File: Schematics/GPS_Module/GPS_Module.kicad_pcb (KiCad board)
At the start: 2 copper layers, 20.3 x 8.4 mm, 86 parts, among them J1 Stack Male Edge Connector, J2 SWD_01x04_Pin, J3 25SH-B-06-TR, J4 25SH-B-06-TR, J6 USB_B_Micro, Q1 AO3400A, SW1 SW_STM_RESET, SW2 SW_STM_BOOT_MODE, U1 STM32F103CBTx, U10 AMS1117-3.3, U2 SAM-M10Q, U3 W25Q128JVS, U4 LM66100DCKR, U5 LM66100DCKR, U6 LM66100DCKR, U7 ACS70331EOLC, U8 LM66100DCKR, U9 ISO1042BQDWVR, Y1 X322516MMB4SI

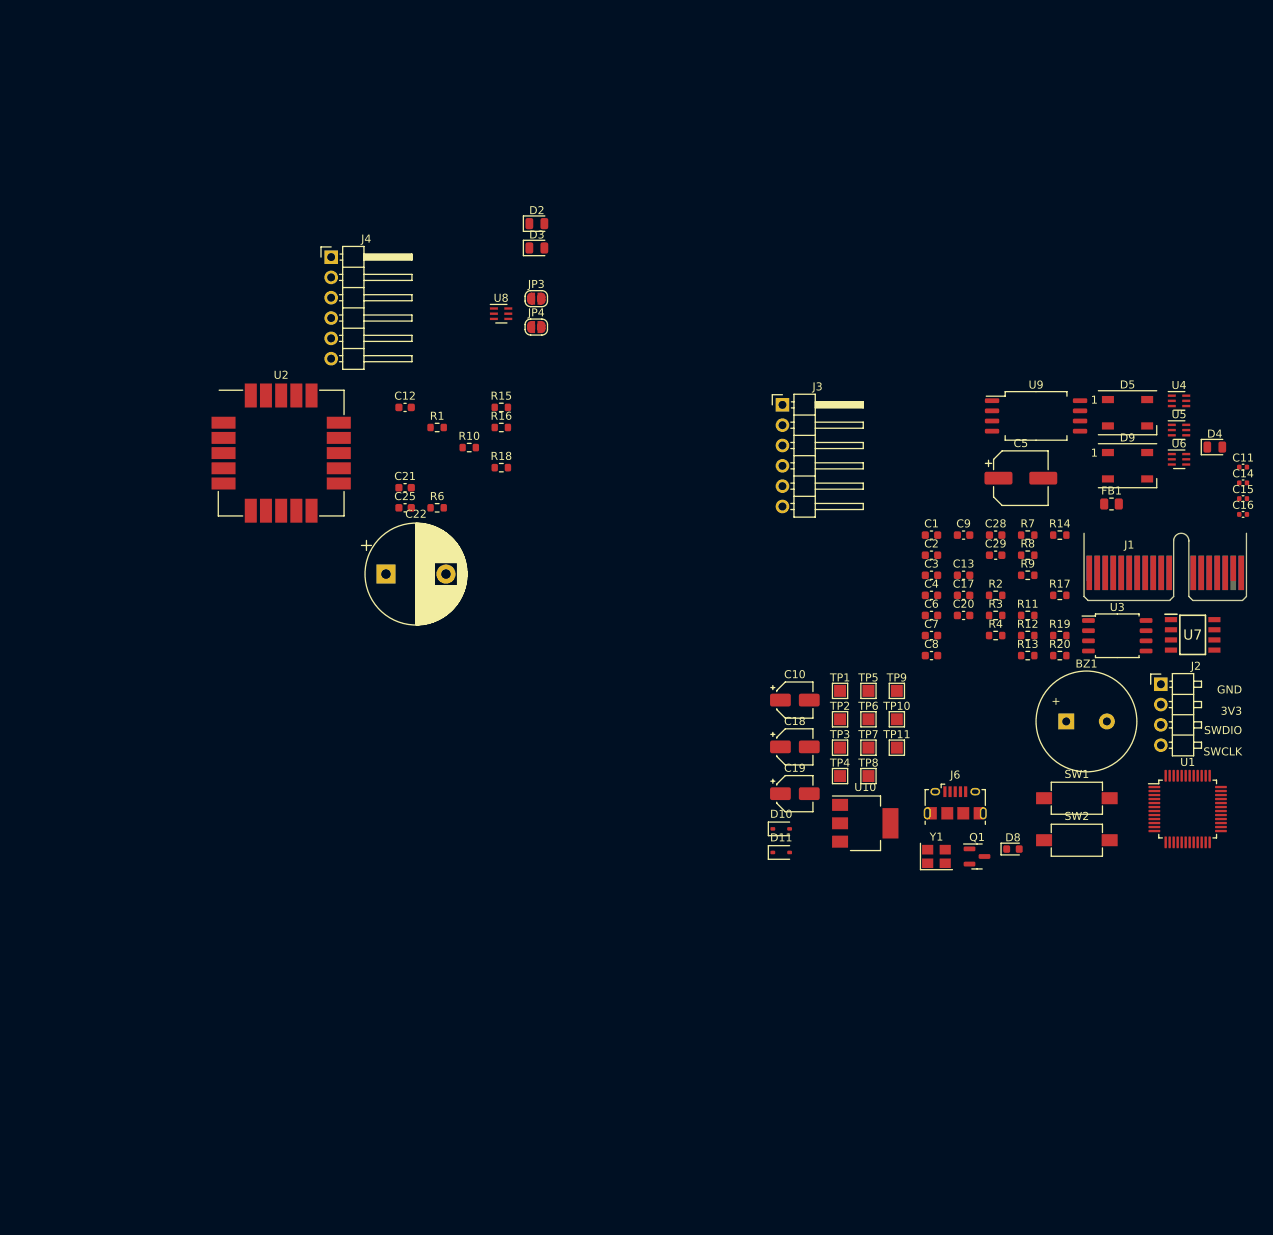
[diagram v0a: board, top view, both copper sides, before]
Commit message: Added PCB template
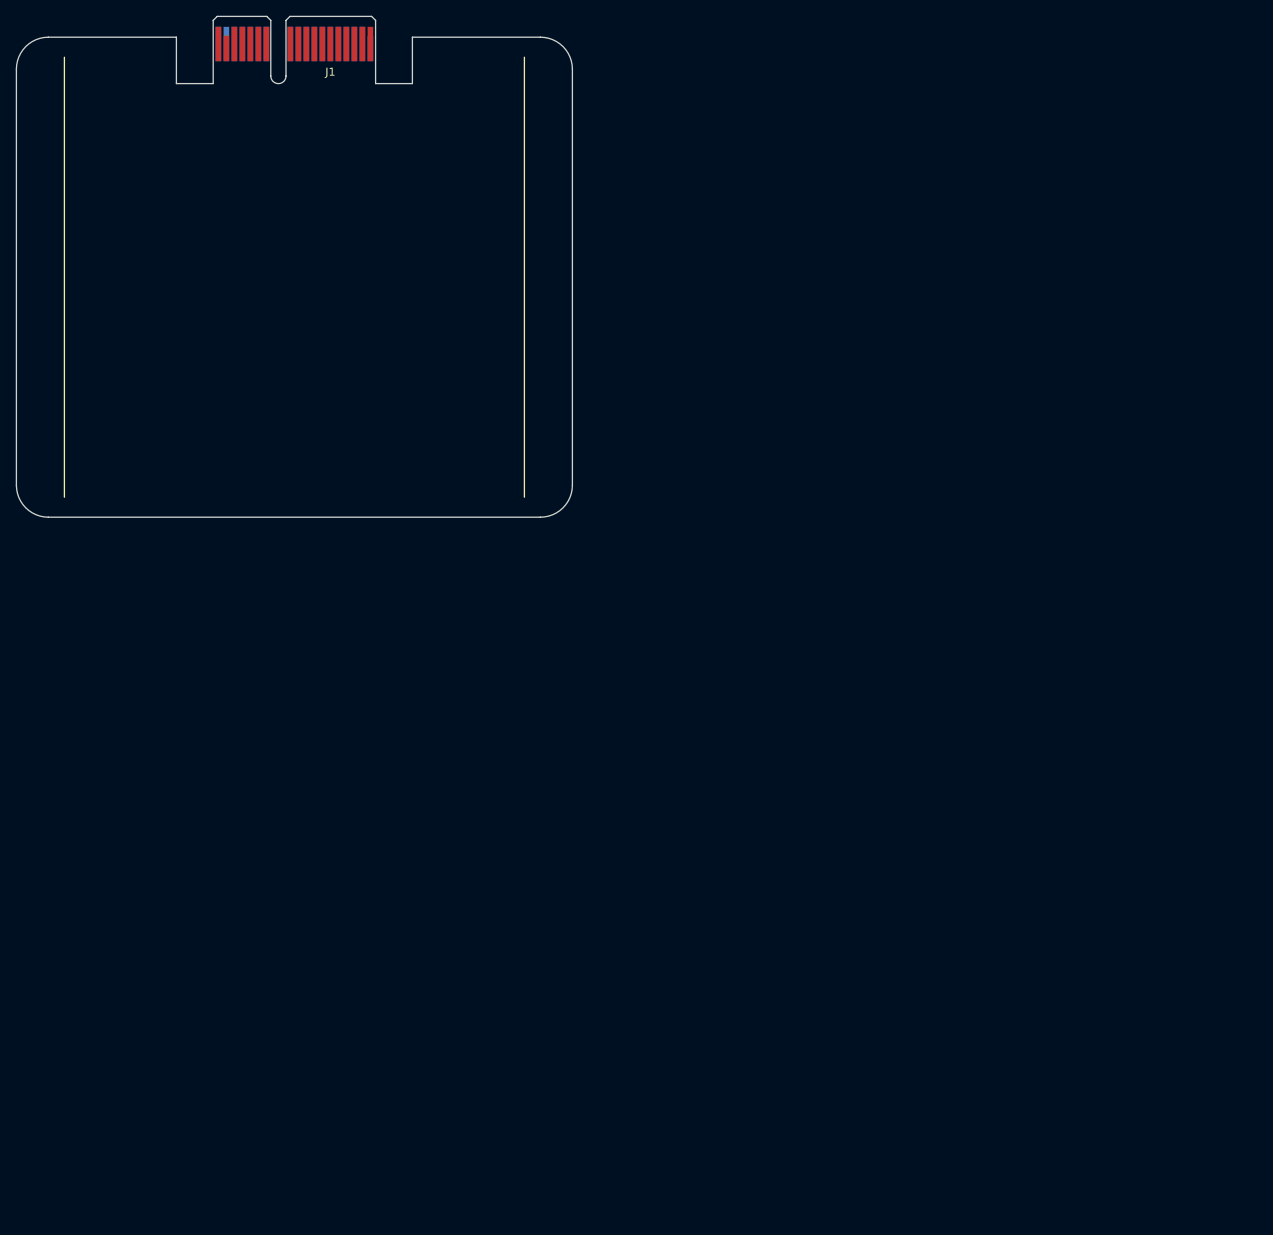
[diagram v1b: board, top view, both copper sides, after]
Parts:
- removed BZ1: PKM13EPYH4000, footprints:Buzzer_12.6x9.5RM5.0
- removed C1, C2, C21, C4: 1uF, Capacitor_SMD:C_0603_1608Metric
- removed C10: 10u, Capacitor_SMD:CP_Elec_4x5.4
- removed C11, C14, C15, C16: 100n, Capacitor_SMD:C_0402_1005Metric
- removed C12, C13, C25, C7: 100nF, Capacitor_SMD:C_0603_1608Metric
- removed C17: 10n, Capacitor_SMD:C_0603_1608Metric
- removed C18, C19: 1uF, Capacitor_SMD:CP_Elec_4x5.4
- removed C20, C3: 10p, Capacitor_SMD:C_0603_1608Metric
- removed C22: 330mF, Capacitor_THT:CP_Radial_D12.5mm_P7.50mm
- removed C28, C29: 10uF, Capacitor_SMD:C_0603_1608Metric
- removed C5: 100uF, Capacitor_SMD:CP_Elec_6.3x5.9
- removed C6: 0.1uF, Capacitor_SMD:C_0603_1608Metric
- removed C8, C9: 0.1u, Capacitor_SMD:C_0603_1608Metric
- removed D10, D11: 1N5819WS, Diode_SMD:D_SOD-323
- removed D2: GREEN, LED_SMD:LED_0805_2012Metric
- removed D3: WHITE, LED_SMD:LED_0805_2012Metric
- removed D4: PWR_LED (GRN), LED_SMD:LED_0805_2012Metric
- removed D5, D9: WS2812B, LED_SMD:LED_WS2812B_PLCC4_5.0x5.0mm_P3.2mm
- removed D8: DB_LED (YLW), LED_SMD:LED_0603_1608Metric
- removed FB1: 100R, Resistor_SMD:R_0805_2012Metric
- removed J2: SWD_01x04_Pin, SWD_Header:SWD_PinHeader_1x04_P2.54mm_Horizontal
- removed J3, J4: 25SH-B-06-TR, Connector_PinHeader_2.54mm:PinHeader_1x06_P2.54mm_Horizontal
- removed J6: USB_B_Micro, Connector_USB:USB_Micro-B_Amphenol_10118194_Horizontal
- removed JP3: ENA_PPS_LED, Jumper:SolderJumper-2_P1.3mm_Open_RoundedPad1.0x1.5mm
- removed JP4: ENA_PWR_LED, Jumper:SolderJumper-2_P1.3mm_Open_RoundedPad1.0x1.5mm
- removed Q1: AO3400A, Package_TO_SOT_SMD:SOT-23
- removed R1, R11, R13, R17, R2, R3: 10k, Resistor_SMD:R_0603_1608Metric
- removed R10, R15, R16, R6: 2.2k, Resistor_SMD:R_0603_1608Metric
- removed R12: 1k, Resistor_SMD:R_0603_1608Metric
- removed R14: 30k, Resistor_SMD:R_0603_1608Metric
- removed R18: 100R, Resistor_SMD:R_0603_1608Metric
- removed R19, R20: 100k, Resistor_SMD:R_0603_1608Metric
- removed R4: 820R, Resistor_SMD:R_0603_1608Metric
- removed R7: 560R, Resistor_SMD:R_0603_1608Metric
- removed R8: 1.5k, Resistor_SMD:R_0603_1608Metric
- removed R9: 510R, Resistor_SMD:R_0603_1608Metric
- removed SW1: SW_STM_RESET, PTS636:PTS636_SK43_SMTR_LFS
- removed SW2: SW_STM_BOOT_MODE, PTS636:PTS636_SK43_SMTR_LFS
- removed TP1: TP_VSTACK, TestPoint:TestPoint_Pad_1.5x1.5mm
- removed TP10: TP_PA1, TestPoint:TestPoint_Pad_1.5x1.5mm
- removed TP11: TP_PA0, TestPoint:TestPoint_Pad_1.5x1.5mm
- removed TP2: TP_VUSB, TestPoint:TestPoint_Pad_1.5x1.5mm
- removed TP3: TP_VSWD, TestPoint:TestPoint_Pad_1.5x1.5mm
- removed TP4: TP_MUX, TestPoint:TestPoint_Pad_1.5x1.5mm
- removed TP5: TP_ISENSE, TestPoint:TestPoint_Pad_1.5x1.5mm
- removed TP6: TP_GND, TestPoint:TestPoint_Pad_1.5x1.5mm
- removed TP7: TP_3V3, TestPoint:TestPoint_Pad_1.5x1.5mm
- removed TP8: TP_BSENSE, TestPoint:TestPoint_Pad_1.5x1.5mm
- removed TP9: TP_PA2, TestPoint:TestPoint_Pad_1.5x1.5mm
- removed U1: STM32F103CBTx, Package_QFP:LQFP-48_7x7mm_P0.5mm
- removed U10: AMS1117-3.3, Package_TO_SOT_SMD:SOT-223-3_TabPin2
- removed U2: SAM-M10Q, RF_GPS:ublox_SAM-M8Q_HandSolder
- removed U3: W25Q128JVS, Package_SO:SOIC-8_5.23x5.23mm_P1.27mm
- removed U4, U5, U6, U8: LM66100DCKR, LMR66100:SC-70-6
- removed U7: ACS70331EOLC, footprints:SOIC127P600X175-8N
- removed U9: ISO1042BQDWVR, ISO1042:SOIC-8 ISO1042BDWV
- removed Y1: X322516MMB4SI, Crystal:Crystal_SMD_3225-4Pin_3.2x2.5mm
- moved J1 111.6 mm to (66.4, 21.0), turned to 180 degrees
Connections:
- J1 pad A1: V_BATT -> V_PSU
- J1 pad A10: unconnected-(J1-BATT_B-PadA10) -> unconnected-(J1-Reserved-PadA10)
- J1 pad A11: unconnected-(J1-GND_B-PadA11) -> unconnected-(J1-Reserved-PadA11)
- J1 pad A12: unconnected-(J1-GND_B-PadA11) -> unconnected-(J1-GND_B-PadA12)
- J1 pad A13: unconnected-(J1-3.3V_B-PadA13) -> DB_LED
- J1 pad A14: unconnected-(J1-GND_B-PadA11) -> unconnected-(J1-Reserved-PadA14)
- J1 pad A15: CAN_H -> unconnected-(J1-Reserved-PadA15)
- J1 pad A16: DB_LED -> unconnected-(J1-Reserved-PadA16)
- J1 pad A2: V_BATT -> V_PSU
- J1 pad A4: GND -> +5V
- J1 pad A5: V_PSU -> +5V
- J1 pad A7: +5V -> unconnected-(J1-3.3V_B-PadA7)
- J1 pad A8: GND -> unconnected-(J1-3.3V_B-PadA7)
- J1 pad A9: unconnected-(J1-BATT_B-PadA10) -> unconnected-(J1-GND_B-PadA12)
- J1 pad B10: unconnected-(J1-BATT_B-PadA10) -> unconnected-(J1-GND_B-PadA12)
- J1 pad B11: unconnected-(J1-GND_B-PadA11) -> unconnected-(J1-GND_B-PadA12)
- J1 pad B12: unconnected-(J1-GND_B-PadA11) -> unconnected-(J1-GND_B-PadA12)
- J1 pad B13: unconnected-(J1-3.3V_B-PadA13) -> CAN_L
- J1 pad B14: unconnected-(J1-GND_B-PadA11) -> CAN_H
- J1 pad B15: CAN_L -> unconnected-(J1-Reserved-PadB15)
- J1 pad B3: GND -> V_BATT
- J1 pad B5: V_PSU -> GND
- J1 pad B7: +5V -> unconnected-(J1-BATT_B-PadB7)
- J1 pad B8: GND -> unconnected-(J1-BATT_B-PadB7)
- J1 pad B9: unconnected-(J1-BATT_B-PadA10) -> unconnected-(J1-BATT_B-PadB7)
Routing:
- added copper zone on In1.Cu, net GND
- added copper zone on In2.Cu, net GND
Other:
- board size 20.3 x 8.4 mm -> 69.5 x 60 mm
- copper layers 2 -> 4
- board text added: "GPS Daughterboard will be in a seperate project"
- board text added: "USE GRID THAT IS SOME MULTIPLE OF 0.1mm (0.1mm, 0.2mm, 0.5mm, 1.0mm, etc)"

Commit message: starting PCB layout
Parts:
- added BZ1: PKM13EPYH4000, footprints:Buzzer_12.6x9.5RM5.0, F.Cu at (31.6, 75.3)
- added C1: 1uF, Capacitor_SMD:C_0603_1608Metric, F.Cu at (29.4, 39.7)
- added C10: 10u, Capacitor_SMD:CP_Elec_4x5.4, F.Cu at (70.4, 110.8)
- added C11: 100n, Capacitor_SMD:C_0402_1005Metric, F.Cu at (77.5, 59.0)
- added C13: 100nF, Capacitor_SMD:C_0603_1608Metric, F.Cu at (89.1, 64.7)
- added C14: 100n, Capacitor_SMD:C_0402_1005Metric, F.Cu at (80.9, 50.5)
- added C15: 100n, Capacitor_SMD:C_0402_1005Metric, F.Cu at (72.5, 47.0)
- added C16: 100n, Capacitor_SMD:C_0402_1005Metric, F.Cu at (68.9, 50.1)
- added C17: 10n, Capacitor_SMD:C_0603_1608Metric, F.Cu at (68.7, 55.2)
- added C18: 1uF, Capacitor_SMD:CP_Elec_4x5.4, F.Cu at (66.1, 59.4)
- added C19: 1uF, Capacitor_SMD:CP_Elec_4x5.4, F.Cu at (66.2, 64.4)
- added C2: 1uF, Capacitor_SMD:C_0603_1608Metric, F.Cu at (29.4, 44.9)
- added C20: 10p, Capacitor_SMD:C_0603_1608Metric, F.Cu at (66.3, 54.2)
- added C28: 10uF, Capacitor_SMD:C_0603_1608Metric, F.Cu at (101.0, 63.2)
- added C29: 10uF, Capacitor_SMD:C_0603_1608Metric, F.Cu at (101.0, 60.5)
- added C3: 10p, Capacitor_SMD:C_0603_1608Metric, F.Cu at (66.3, 51.0)
- added C4: 1uF, Capacitor_SMD:C_0603_1608Metric, F.Cu at (29.5, 50.2)
- added C5: 100uF, Capacitor_SMD:CP_Elec_6.3x5.9, F.Cu at (92.0, 93.5)
- added C6: 0.1uF, Capacitor_SMD:C_0603_1608Metric, F.Cu at (94.8, 100.9)
- added C7: 100nF, Capacitor_SMD:C_0603_1608Metric, F.Cu at (34.6, 158.7)
- added C8: 0.1u, Capacitor_SMD:C_0603_1608Metric, F.Cu at (71.1, 43.4)
- added C9: 0.1u, Capacitor_SMD:C_0603_1608Metric, F.Cu at (71.2, 27.8)
- added D10: 1N5819WS, Diode_SMD:D_SOD-323, F.Cu at (42.4, 69.4)
- added D11: 1N5819WS, Diode_SMD:D_SOD-323, F.Cu at (42.4, 73.0)
- added D4: PWR_LED (GRN), LED_SMD:LED_0805_2012Metric, F.Cu at (107.0, 92.8)
- added D5: WS2812B, LED_SMD:LED_WS2812B_PLCC4_5.0x5.0mm_P3.2mm, F.Cu at (121.1, 38.0)
- added D8: DB_LED (YLW), LED_SMD:LED_0603_1608Metric, F.Cu at (128.8, 37.7)
- added D9: WS2812B, LED_SMD:LED_WS2812B_PLCC4_5.0x5.0mm_P3.2mm, F.Cu at (113.0, 38.0)
- added FB1: 100R, Resistor_SMD:R_0805_2012Metric, F.Cu at (70.5, 61.5)
- added J2: SWD_01x04_Pin, SWD_Header:SWD_PinHeader_1x04_P2.54mm_Horizontal, F.Cu at (81.0, 37.8)
- added J3: 25SH-B-06-TR, Connector_PinHeader_2.54mm:PinHeader_1x06_P2.54mm_Horizontal, F.Cu at (65.2, 69.6)
- added J6: USB_B_Micro, Connector_USB:USB_Micro-B_Amphenol_10118194_Horizontal, F.Cu at (88.9, 51.7)
- added Q1: AO3400A, Package_TO_SOT_SMD:SOT-23, F.Cu at (32.6, 62.1)
- added R11: 10k, Resistor_SMD:R_0603_1608Metric, F.Cu at (36.4, 60.8)
- added R12: 1k, Resistor_SMD:R_0603_1608Metric, F.Cu at (40.1, 71.3)
- added R13: 10k, Resistor_SMD:R_0603_1608Metric, F.Cu at (76.8, 68.9)
- added R14: 10k, Resistor_SMD:R_0603_1608Metric, F.Cu at (67.1, 104.9)
- added R19: 100k, Resistor_SMD:R_0603_1608Metric, F.Cu at (56.9, 132.4)
- added R2: 10k, Resistor_SMD:R_0603_1608Metric, F.Cu at (30.9, 155.4)
- added R20: 100k, Resistor_SMD:R_0603_1608Metric, F.Cu at (71.5, 157.1)
- added R3: 10k, Resistor_SMD:R_0603_1608Metric, F.Cu at (89.1, 67.7)
- added R4: 820R, Resistor_SMD:R_0603_1608Metric, F.Cu at (102.8, 92.9)
- added R5: 30k, Resistor_SMD:R_0603_1608Metric, F.Cu at (67.1, 100.9)
- added R7: 560R, Resistor_SMD:R_0603_1608Metric, F.Cu at (128.8, 41.0)
- added R8: 1.5k, Resistor_SMD:R_0603_1608Metric, F.Cu at (84.4, 50.8)
- added R9: 510R, Resistor_SMD:R_0603_1608Metric, F.Cu at (36.4, 63.9)
- added SW1: SW_STM_RESET, PTS636:PTS636_SK43_SMTR_LFS, F.Cu at (30.9, 162.8)
- added SW2: SW_STM_BOOT_MODE, PTS636:PTS636_SK43_SMTR_LFS, F.Cu at (53.4, 128.3)
- added TP1: TP_VSTACK, TestPoint:TestPoint_Pad_1.5x1.5mm, F.Cu at (32.4, 37.5)
- added TP10: TP_PA1, TestPoint:TestPoint_Pad_1.5x1.5mm, F.Cu at (43.0, 99.8)
- added TP11: TP_PA0, TestPoint:TestPoint_Pad_1.5x1.5mm, F.Cu at (39.5, 99.8)
- added TP2: TP_VUSB, TestPoint:TestPoint_Pad_1.5x1.5mm, F.Cu at (32.4, 42.6)
- added TP3: TP_VSWD, TestPoint:TestPoint_Pad_1.5x1.5mm, F.Cu at (32.4, 47.9)
- added TP4: TP_MUX, TestPoint:TestPoint_Pad_1.5x1.5mm, F.Cu at (39.7, 44.7)
- added TP5: TP_ISENSE, TestPoint:TestPoint_Pad_1.5x1.5mm, F.Cu at (98.3, 97.1)
- added TP6: TP_GND, TestPoint:TestPoint_Pad_1.5x1.5mm, F.Cu at (105.5, 100.6)
- added TP7: TP_3V3, TestPoint:TestPoint_Pad_1.5x1.5mm, F.Cu at (99.6, 110.2)
- added TP8: TP_BSENSE, TestPoint:TestPoint_Pad_1.5x1.5mm, F.Cu at (74.7, 60.4)
- added TP9: TP_PA2, TestPoint:TestPoint_Pad_1.5x1.5mm, F.Cu at (46.6, 99.8)
- added U1: STM32F103CBTx, Package_QFP:LQFP-48_7x7mm_P0.5mm, F.Cu at (74.9, 53.0)
- added U10: AMS1117-3.3, Package_TO_SOT_SMD:SOT-223-3_TabPin2, F.Cu at (101.7, 55.2)
- added U3: W25Q128JVS, Package_SO:SOIC-8_5.23x5.23mm_P1.27mm, F.Cu at (83.0, 67.5)
- added U4: LM66100DCKR, LMR66100:SC-70-6_Handsoldering, F.Cu at (33.3, 40.0)
- added U5: LM66100DCKR, LMR66100:SC-70-6_Handsoldering, F.Cu at (33.3, 45.2)
- added U6: LM66100DCKR, LMR66100:SC-70-6_Handsoldering, F.Cu at (33.3, 50.5)
- added U7: ACS70331EOLC, footprints:SOIC127P600X175-8N, F.Cu at (98.9, 103.4)
- added U9: ISO1042BQDWVR, ISO1042:SOIC-8 ISO1042BDWV, F.Cu at (73.8, 35.5)
- added Y1: X322516MMB4SI, Crystal:Crystal_SMD_3225-4Pin_3.2x2.5mm, F.Cu at (63.6, 52.5)
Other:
- board size 69.5 x 60 mm -> 69.5 x 97.3 mm
- board text removed: "GPS Daughterboard will be in a seperate project"
